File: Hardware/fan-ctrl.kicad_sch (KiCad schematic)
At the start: 31 parts, among them Q1 AO3401A, U1 STM32G070RBT6, U2 826629-3, U3 826629-3, U4 MP2359DT-LF-Z, Y1 Crystal_GND24

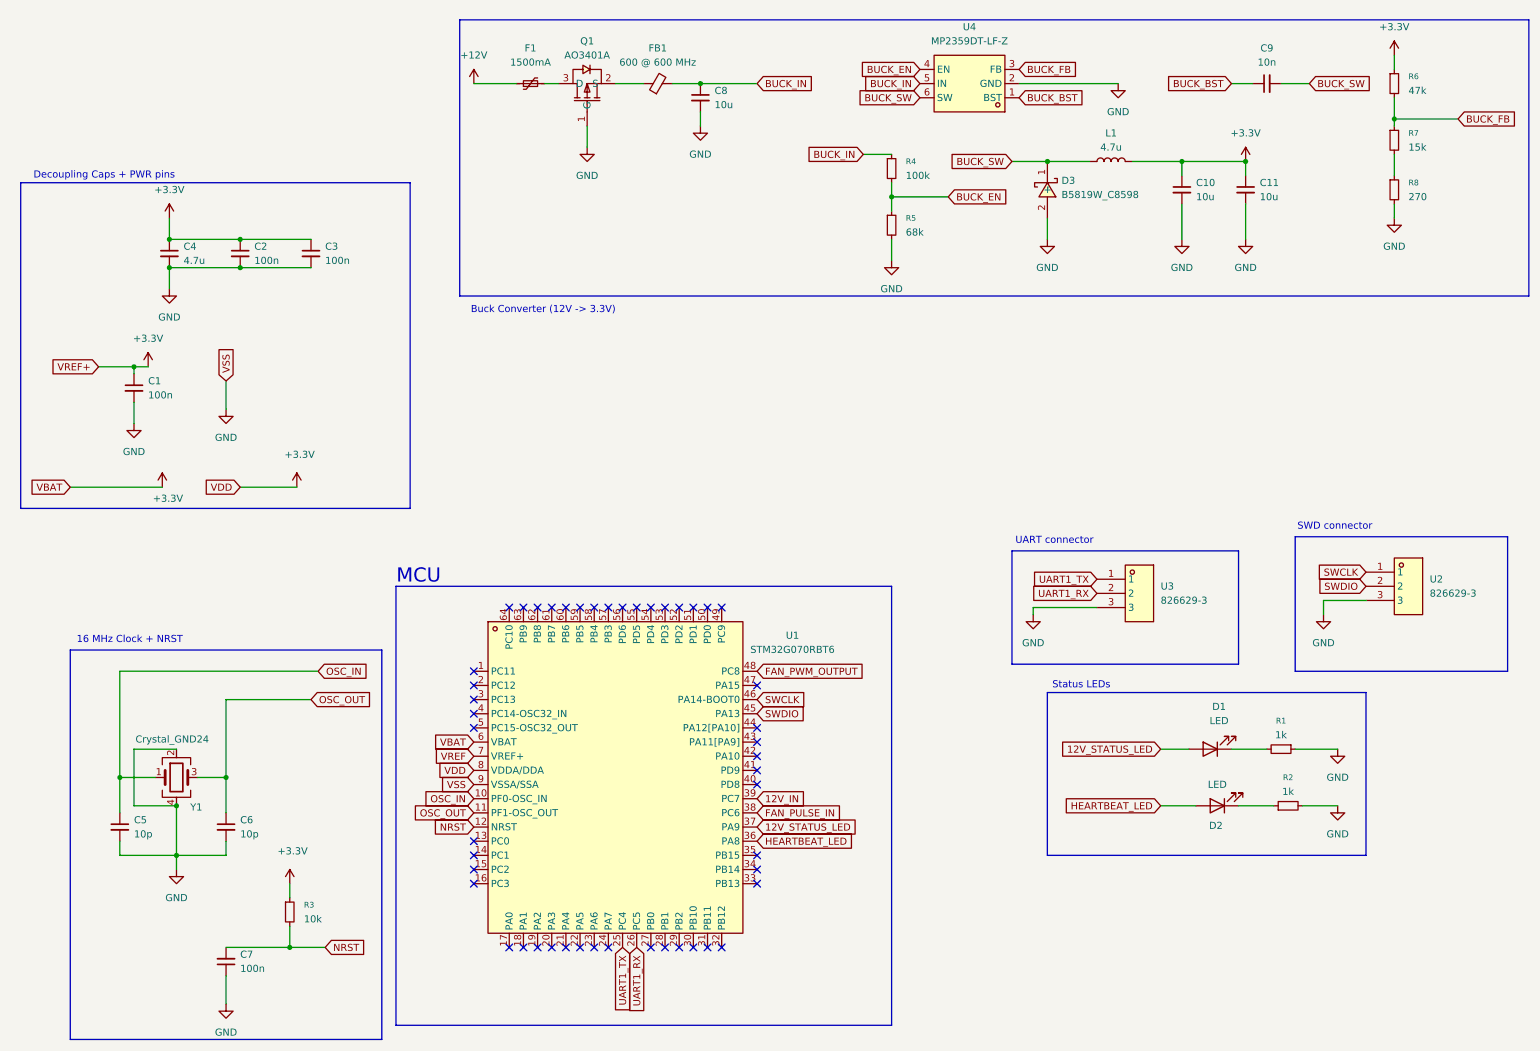
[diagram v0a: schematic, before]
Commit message: Update buck converter circuit (5V output), add switching linear regulator for 3.3V output, add N-channel MOSFET for 5V PWM control
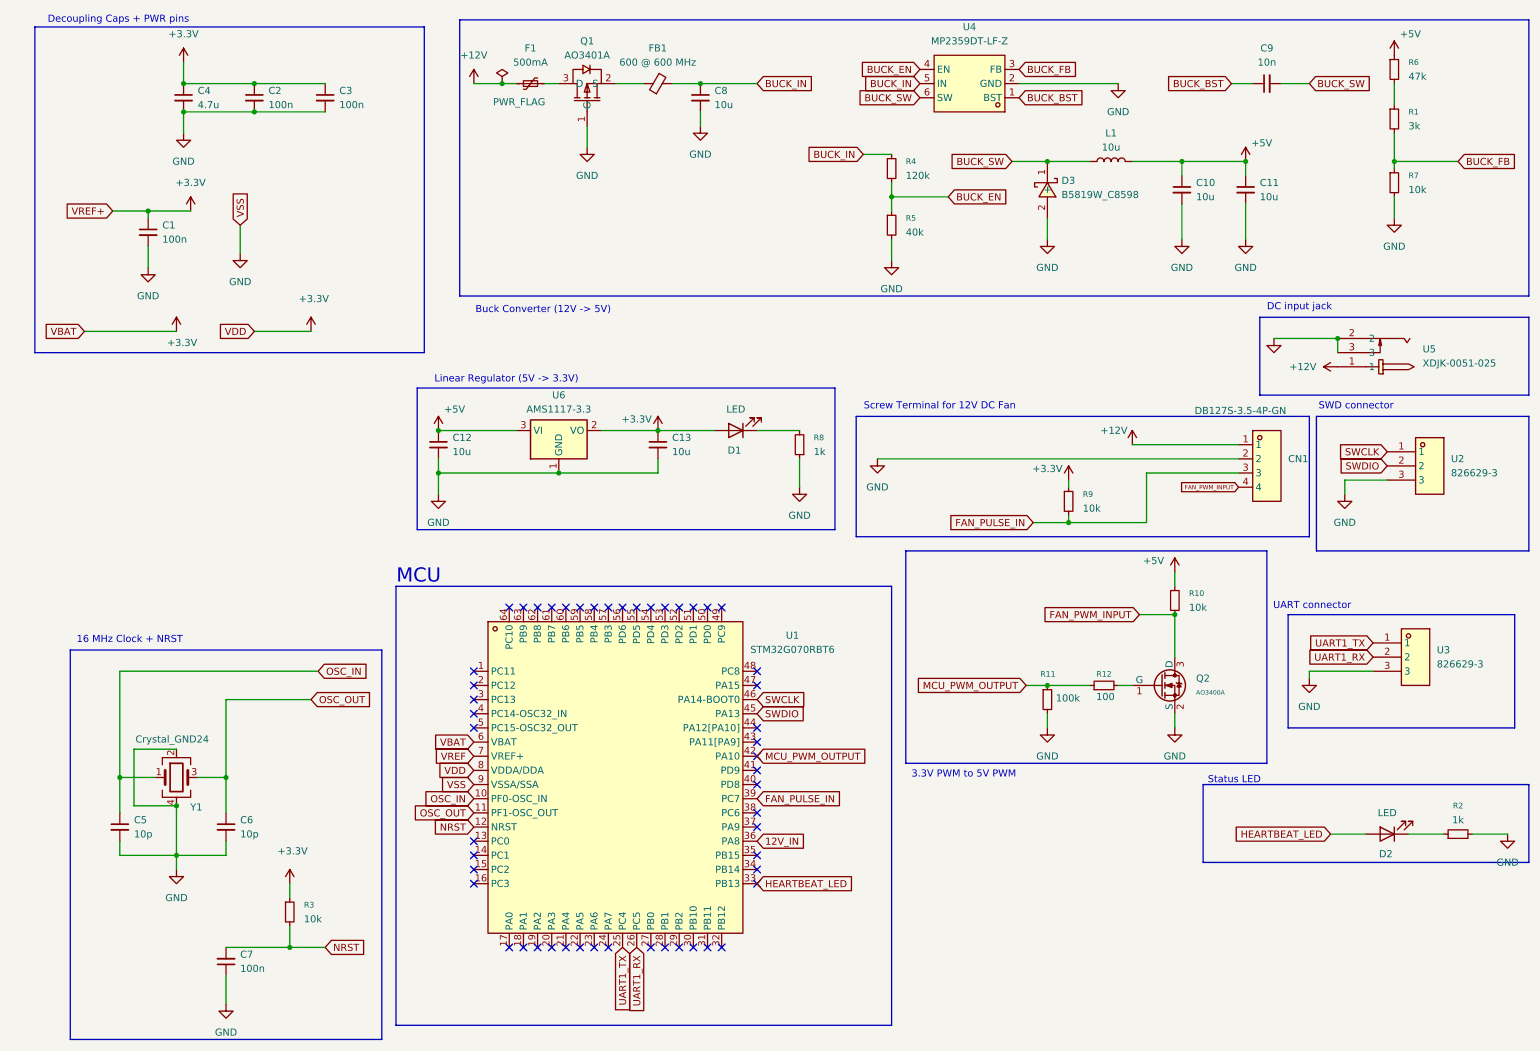
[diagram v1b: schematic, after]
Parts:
- added C12, C13: 10u, symbol Device:C_Small
- added CN1: DB127S-3.5-4P-GN, easyeda2kicad:CONN-TH_4P-P3.50_DIBO_DB127S-3.5-4P-GN, symbol easyeda2kicad:DB127S-3.5-4P-GN
- added Q2: AO3400A, PCM_JLCPCB:Q_SOT-23, symbol PCM_JLCPCB-Transistors:NMOS,AO3400A
- added R10, R9: 10k, symbol Device:R_Small
- added R11: 100k, symbol Device:R_Small
- added R12: 100, symbol Device:R_Small
- added U5: XDJK-0051-025, easyeda2kicad:DC-IN-TH_XDJK-0051-025, symbol easyeda2kicad:XDJK-0051-025
- added U6: AMS1117-3.3, Package_TO_SOT_SMD:SOT-223-3_TabPin2, symbol Regulator_Linear:AMS1117-3.3
- F1: value 1500mA -> 500mA
- L1: value 4.7u -> 10u
- R1: value 1k -> 3k
- R4: value 100k -> 120k
- R5: value 68k -> 40k
- R7: value 15k -> 10k
- R8: value 270 -> 1k
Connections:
- net +12V: now also CN1.1, U5.1
- net +3.3V: now also D1.2 (A), C13.1, R9.1, U6.2 (VO); no longer C10.1, C11.1, L1.2, R6.1
- net 12V_IN: now also U1.36 (PA8); no longer U1.39 (PC7)
- net BUCK_FB: now also R1.2; no longer R6.2
- net FAN_PULSE_IN: now also U1.39 (PC7), CN1.3, R9.2; no longer U1.38 (PC6)
- net GND: now also R7.2, R8.1, C12.2, C13.2, CN1.2, Q2.2 (S), R11.2, U5.2, U5.3, U6.1 (GND); no longer R1.1, R8.2
- net HEARTBEAT_LED: now also U1.33 (PB13); no longer U1.36 (PA8)
- net at D1.1 (K): now also R8.2; no longer R1.2
- net MCU_PWM_OUTPUT: now reaches U1.42 (PA10)
- net MCU_PWM_OUTPUT: now also R11.1, R12.1
- net 12V_STATUS_LED: no longer names the net of U1.37 (PA9)
- net 12V_STATUS_LED: no longer D1.2 (A)
- net FAN_PWM_OUTPUT: no longer names the net of U1.48 (PC8)
- new net: R1.1, R6.2
- new net: Q2.1 (G), R12.2
- new net +5V: C10.1, C11.1, C12.1, L1.2, R10.1, R6.1, U6.3 (VI)
- new net FAN_PWM_INPUT: CN1.4, Q2.3 (D), R10.2
- no-connect marks 48 -> 51
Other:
- note added: "3.3V PWM to 5V PWM"
- note added: "Buck Converter (12V -> 5V)"
- note added: "DC input jack"
- note added: "Linear Regulator (5V -> 3.3V)"
- note added: "Screw Terminal for 12V DC Fan"
- note added: "Status LED"
- note removed: "Buck Converter (12V -> 3.3V)"
- note removed: "Status LEDs"
- moved on the sheet: C1, C2, C3, C4, D2, R2, R6, R7, U2, U3

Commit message: Add mounting holes, test points, initial footprint assignment, next up:review design and buck converter output, review available footprints in JLCPCB
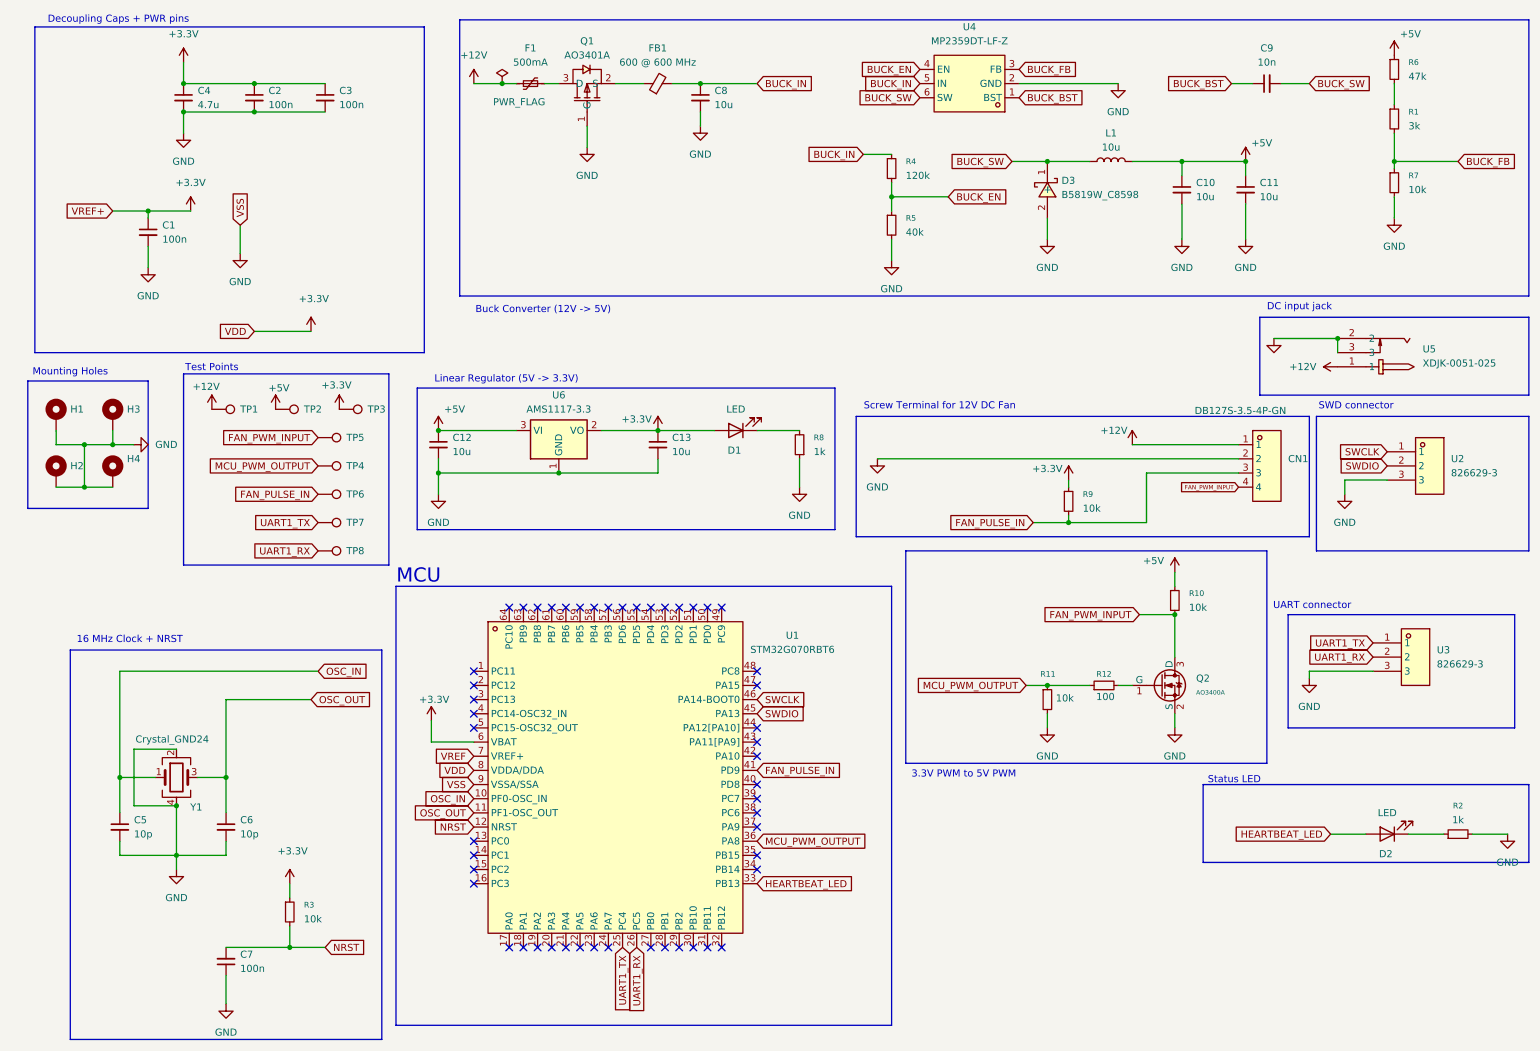
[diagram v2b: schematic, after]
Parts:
- added H1, H2, H3, H4: MountingHole_Pad, MountingHole:MountingHole_4.3mm_M4_Pad_Via, symbol Mechanical:MountingHole_Pad
- added TP1, TP2, TP3, TP4, TP5, TP6, TP7, TP8: TestPoint, TestPoint:TestPoint_Pad_D2.5mm, symbol Connector:TestPoint
- C1, C2, C3, C4, C5, C6, C7: footprint (none) -> Capacitor_SMD:C_0402_1005Metric
- C10, C11, C12, C13, C8, C9: footprint (none) -> Capacitor_SMD:C_1206_3216Metric
- D1, D2: footprint (none) -> LED_SMD:LED_0603_1608Metric
- F1: footprint (none) -> Fuse:Fuse_1206_3216Metric
- FB1, L1: footprint (none) -> Inductor_SMD:L_1206_3216Metric
- R1, R10, R4, R5, R6, R7, R9: footprint (none) -> PCM_JLCPCB:R_0603
- R11: value 100k -> 10k; footprint (none) -> PCM_JLCPCB:R_0402
- R12, R2, R3, R8: footprint (none) -> PCM_JLCPCB:R_0402
- Y1: footprint (none) -> Crystal:Crystal_SMD_3225-4Pin_3.2x2.5mm
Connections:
- net 12V_IN is gone; now on net MCU_PWM_OUTPUT: U1.36 (PA8)
- net +12V: now also TP1.1
- net +3.3V: now also TP3.1
- net +5V: now also TP2.1
- net FAN_PULSE_IN: now also U1.41 (PD9), TP6.1; no longer U1.39 (PC7)
- net FAN_PWM_INPUT: now also TP5.1
- net GND: now also H1.1, H2.1, H3.1, H4.1
- net MCU_PWM_OUTPUT: now also TP4.1; no longer U1.42 (PA10)
- net UART1_RX: now also TP8.1
- net UART1_TX: now also TP7.1
- no-connect marks 51 -> 50
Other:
- note added: "Mounting Holes"
- note added: "Test Points"

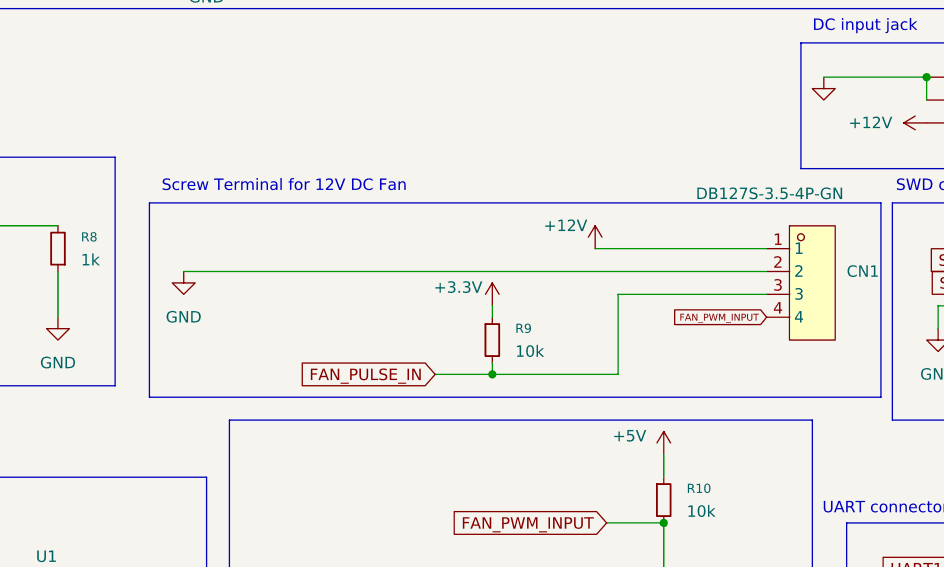
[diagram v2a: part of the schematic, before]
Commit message: Component placement, board edge cuts, adjust some footprints, testpoints, silkscreen for connectors and testpoints, next: review footprints JLCPCB before routing
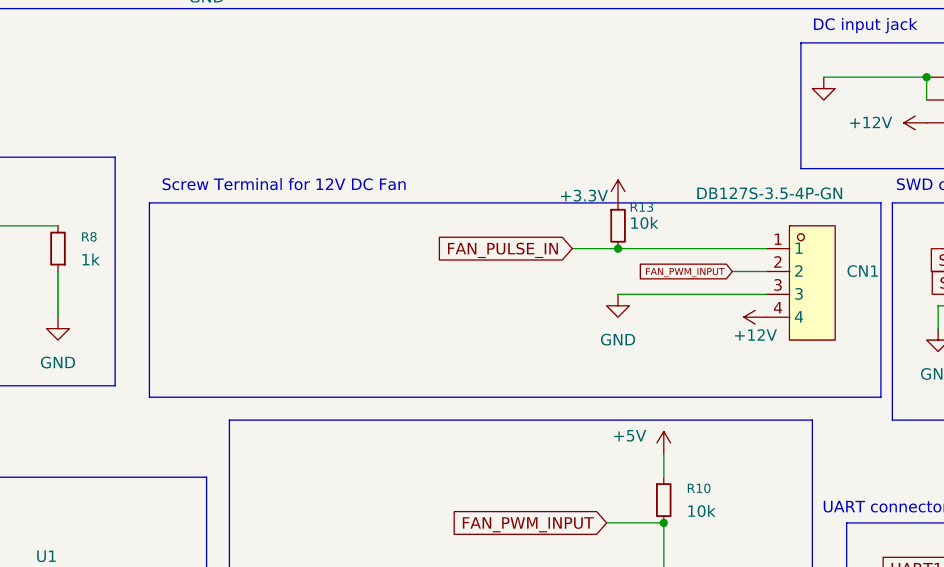
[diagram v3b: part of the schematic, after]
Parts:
- removed R9: 10k, PCM_JLCPCB:R_0603, symbol Device:R_Small
- added R13: 10k, PCM_JLCPCB:R_0603, symbol Device:R_Small
- D1: footprint LED_SMD:LED_0603_1608Metric -> LED_SMD:LED_0805_2012Metric
- D2: footprint LED_SMD:LED_0603_1608Metric -> LED_SMD:LED_0402_1005Metric
- H1, H2, H3, H4: footprint MountingHole:MountingHole_4.3mm_M4_Pad_Via -> MountingHole:MountingHole_2.2mm_M2_Pad_Via
- TP4: footprint TestPoint:TestPoint_Pad_D2.5mm -> TestPoint:TestPoint_Pad_D1.0mm
- TP7, TP8: footprint TestPoint:TestPoint_Pad_D2.5mm -> TestPoint:TestPoint_Pad_D1.5mm
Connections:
- net +12V: now also CN1.4; no longer CN1.1
- net +3.3V: now also R13.1
- net FAN_PULSE_IN: now also CN1.1, R13.2; no longer CN1.3
- net FAN_PWM_INPUT: now also CN1.2; no longer CN1.4
- net GND: now also CN1.3; no longer CN1.2

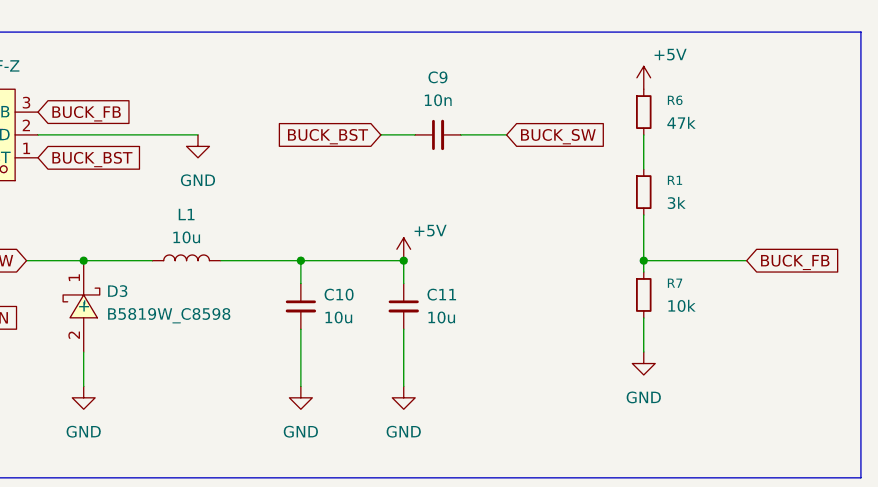
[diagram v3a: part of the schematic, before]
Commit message: Update buck converter circuit, standard R values for close 5V output, double-checked footprints available in JLCPCB
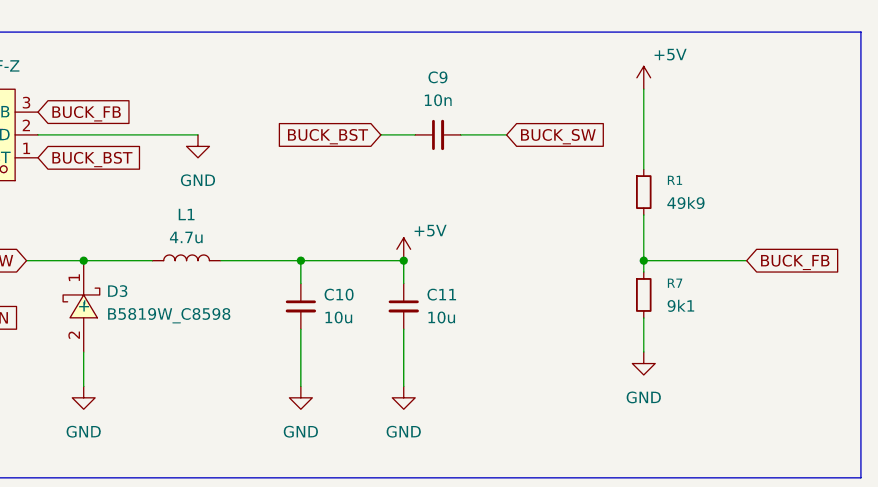
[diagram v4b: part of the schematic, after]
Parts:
- removed R6: 47k, PCM_JLCPCB:R_0603, symbol Device:R_Small
- L1: value 10u -> 4.7u
- R1: value 3k -> 49k9
- R7: value 10k -> 9k1
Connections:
- net +5V: now also R1.1
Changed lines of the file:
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@@
 	(wire
 		(pts
-			(xy 259.08 25.4) (xy 259.08 29.21)
+			(xy 259.08 20.32) (xy 259.08 29.21)
 		)
 		(stroke
@@
 	(symbol
 		(lib_id "Device:R_Small")
-		(at 259.08 22.86 0)
-		(unit 1)
-		(exclude_from_sim no)
-		(in_bom yes)
-		(on_board yes)
-		(dnp no)
-		(fields_autoplaced yes)
-		(property "Reference" "R6"
-			(at 261.62 21.5899 0)
-			(effects
-				(font
-					(size 1.016 1.016)
-				)
-				(justify left)
-			)
-		)
-		(property "Value" "47k"
-			(at 261.62 24.1299 0)
-			(effects
-				(font
-					(size 1.27 1.27)
-				)
-				(justify left)
-			)
-		)
-		(property "Footprint" "PCM_JLCPCB:R_0603"
-			(at 259.08 22.86 0)
-			(effects
-				(font
-					(size 1.27 1.27)
-				)
-				(hide yes)
-			)
-		)
-		(property "Datasheet" "~"
-			(at 259.08 22.86 0)
-			(effects
-				(font
-					(size 1.27 1.27)
-				)
-				(hide yes)
-			)
-		)
-		(property "Description" "Resistor, small symbol"
-			(at 259.08 22.86 0)
-			(effects
-				(font
-					(size 1.27 1.27)
-				)
-				(hide yes)
-			)
-		)
-		(pin "1"
-		)
-		(pin "2"
-		)
-		(instances
-			(project "fan-ctrl"
-				(path "/3b32e9df-6978-4cdc-9438-caa67c4a1546"
-					(reference "R6")
-					(unit 1)
-				)
-			)
-		)
-	)
-	(symbol
-		(lib_id "Device:R_Small")
 		(at 207.01 133.35 90)
 		(unit 1)
@@
 			)
 		)
-		(property "Value" "3k"
+		(property "Value" "49k9"
 			(at 261.62 33.0199 0)
 			(effects
@@
 			)
 		)
-		(property "Value" "10k"
+		(property "Value" "9k1"
 			(at 261.62 44.4499 0)
 			(effects
@@
 			)
 		)
-		(property "Value" "10u"
+		(property "Value" "4.7u"
 			(at 208.28 36.83 90)
 			(effects
